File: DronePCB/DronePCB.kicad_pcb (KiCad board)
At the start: 4 copper layers, 158 x 68 mm, 167 parts, among them J1 VBUS, J10 SysPower, J2 PD_SCL, J3 PD_SDA, J4 SysPower, J5 UART, J6 5V, J7 3V3, J8 USB_C_Receptacle_PowerOnly_6P, J9 Batt, M1 Motor_DC, M2 Motor_DC, Q1 AO3400A, Q2 AO3400A, Q3 AO3400A, Q4 AO3400A, Q5 AO3400A, Q6 AO3401A, Q7 AO3401A, Q8 AO3401A, Q9 AO3401A, U1 RASPBERRY_PI_ZERO_2_W, U10 DRV8231DDAR, U2 CC1101RGPR, U3 BQ24725A, U4 CYPD3177-24LQXQT, U5 DMP3098LSD-13, U6 DMP3098LSD-13, U7 LMR33630BDDA, U8 TSOP45xx, U9 DRV8231DDAR, Y1 NX3225GA

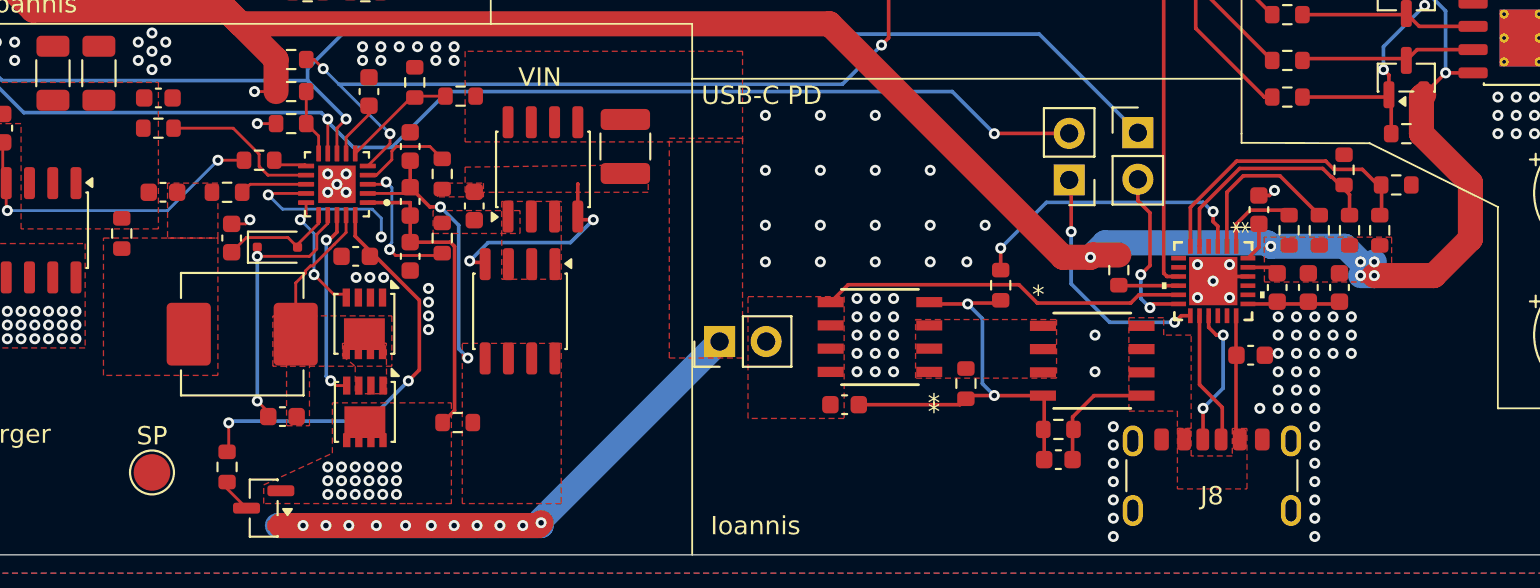
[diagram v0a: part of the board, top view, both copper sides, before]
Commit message: slight pcb tweaks
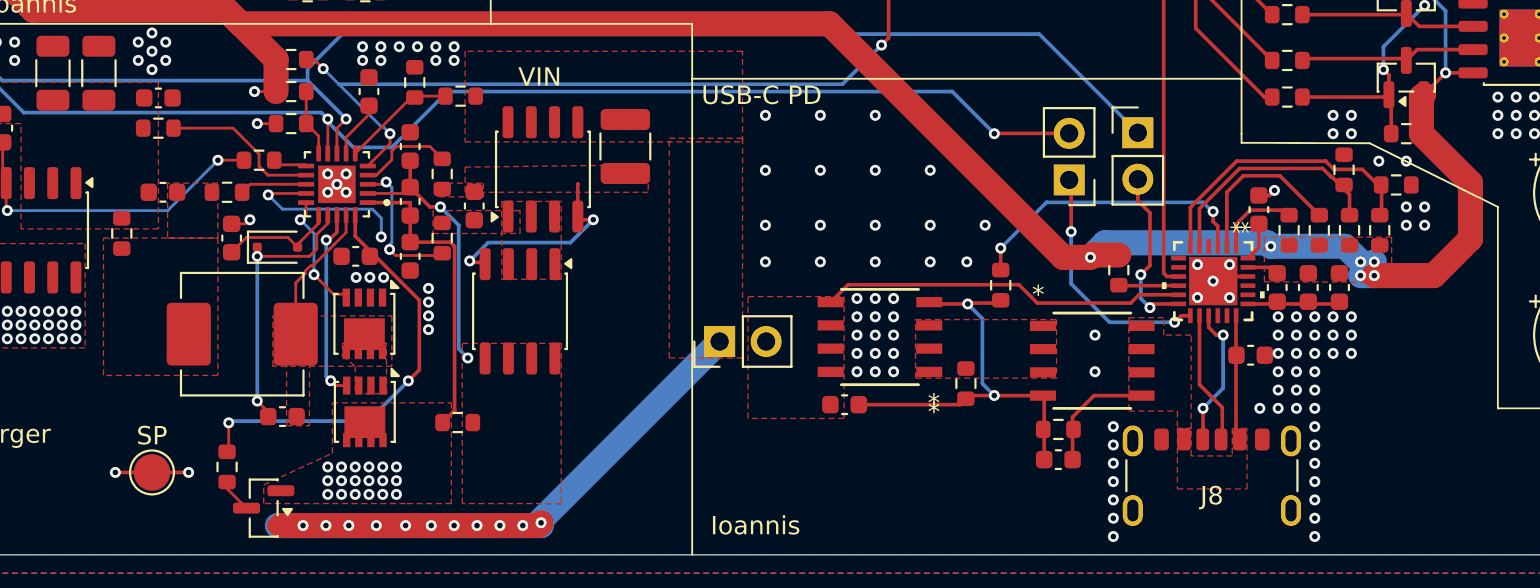
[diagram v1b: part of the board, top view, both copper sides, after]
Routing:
- net /Battery Charger/SystemPower: track 16.9 -> 20.9 mm, vias 36 -> 38
- net GND: vias 386 -> 396
